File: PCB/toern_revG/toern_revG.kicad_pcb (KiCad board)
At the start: 4 copper layers, 160 x 71 mm, 97 parts, among them IC1 BQ24075TRGTR, J1 AudioJack3_Switch, J10 Conn_01x02, J11 Conn_01x05, J11.5 Conn_01x05, J12 Conn_01x05, J13 Conn_01x05, J14 Conn_01x05, J15 Conn_01x05, J16 BATTERY, J17 AudioJack3_Ground, J3 AudioJack3_Ground, J4 USB_C_Receptacle_USB2.0, J5 AudioJack3_Switch, J6 AudioJack3_Switch, J7 AudioJack3_Switch, J8 Micro_SD_Card, J9 Conn_01x03, U1 SPX3819M5-L-3-3, U10 01x05 Connector_PinSocket_2.5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, U11 01x05 Connector_PinSocket_2.5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, U12 01x05 Connector_PinSocket_2.5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, U13 PAM8403D, U2 SPX3819M5-L-1-8, U3 SGTL5000XNBA3, U4 TLP2361V4_E, U5 74LVC2G14, U6 Teensy4.1, U7 SPX3819M5-L-3-3, U9 01x05 Connector_PinSocket_2.5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

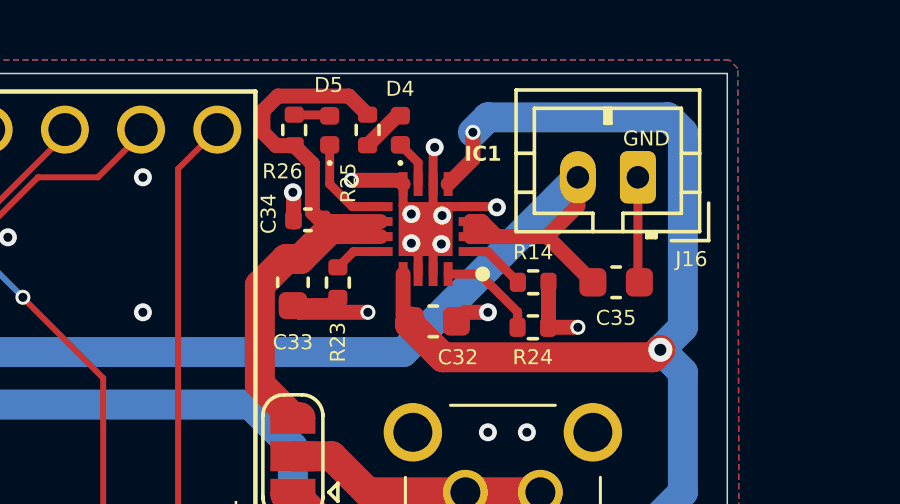
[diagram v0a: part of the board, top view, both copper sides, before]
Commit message: fixes for HD Displays 32x16
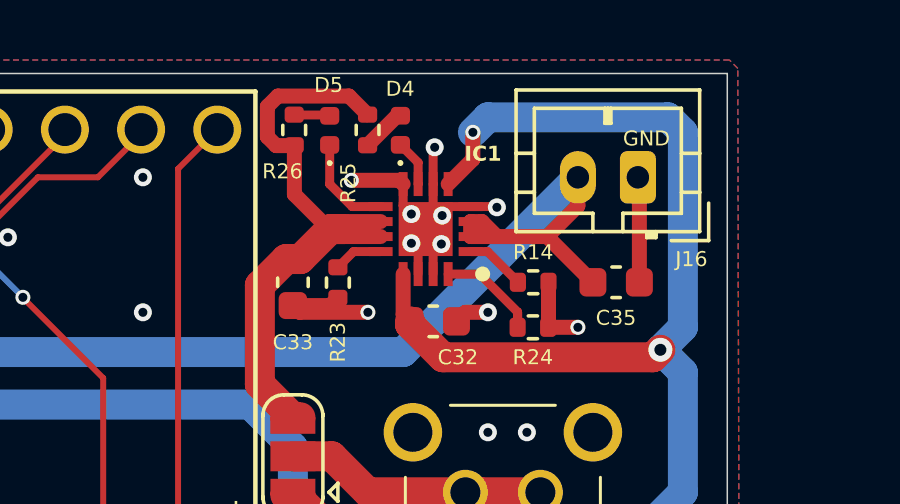
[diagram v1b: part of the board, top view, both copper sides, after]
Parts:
- removed C34: 100nF, Capacitor_SMD:C_0402_1005Metric
- C36: value 470µF -> 22µF
- D4: value Green -> Red
- D5: value Green -> Yellow
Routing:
- net GND: track 134.2 -> 133.3 mm, vias 157 -> 156
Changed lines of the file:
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@@
 			)
 		)
-		(property "lcsc#" "C19666 "
+		(property "lcsc#" "C1705"
 			(at 0 0 270)
 			(unlocked yes)
@@
 		)
 	)
-	(footprint "Capacitor_SMD:C_0402_1005Metric"
-		(layer "F.Cu")
-		(at 177 29.917727 180)
-		(descr "Capacitor SMD 0402 (1005 Metric), square (rectangular) end terminal, IPC-7351 nominal, (Body size source: IPC-SM-782 page 76, https://www.pcb-3d.com/wordpress/wp-content/uploads/ipc-sm-782a_amendment_1_and_2.pdf), generated with kicad-footprint-generator")
-		(tags "capacitor")
-		(property "Reference" "C34"
-			(at 1.308509 0.200909 270)
-			(layer "F.SilkS")
-			(effects
-				(font
-					(size 0.5 0.5)
-					(thickness 0.125)
-				)
-			)
-		)
-		(property "Value" "100nF"
-			(at 0 1.16 0)
-			(layer "F.Fab")
-			(effects
-				(font
-					(size 1 1)
-					(thickness 0.15)
-				)
-			)
-		)
-		(property "Datasheet" ""
-			(at 0 0 0)
-			(layer "F.Fab")
-			(hide yes)
-			(effects
-				(font
-					(size 1.27 1.27)
-					(thickness 0.15)
-				)
-			)
-		)
-		(property "Description" "Unpolarized capacitor, small symbol"
-			(at 0 0 0)
-			(layer "F.Fab")
-			(hide yes)
-			(effects
-				(font
-					(size 1.27 1.27)
-					(thickness 0.15)
-				)
-			)
-		)
-		(property "lcsc#" "C1525"
-			(at 0 0 270)
-			(unlocked yes)
-			(layer "F.Fab")
-			(hide yes)
-			(effects
-				(font
-					(size 1 1)
-					(thickness 0.15)
-				)
-			)
-		)
-		(property ki_fp_filters "C_*")
-		(sheetname "/")
-		(sheetfile "toern_revG.kicad_sch")
-		(attr smd)
-		(fp_line
-			(start -0.107836 0.36)
-			(end 0.107836 0.36)
-			(stroke
-				(width 0.12)
-				(type solid)
-			)
-			(layer "F.SilkS")
-		)
-		(fp_line
-			(start -0.107836 -0.36)
-			(end 0.107836 -0.36)
-			(stroke
-				(width 0.12)
-				(type solid)
-			)
-			(layer "F.SilkS")
-		)
-		(fp_line
-			(start 0.91 0.46)
-			(end -0.91 0.46)
-			(stroke
-				(width 0.05)
-				(type solid)
-			)
-			(layer "F.CrtYd")
-		)
-		(fp_line
-			(start 0.91 -0.46)
-			(end 0.91 0.46)
-			(stroke
-				(width 0.05)
-				(type solid)
-			)
-			(layer "F.CrtYd")
-		)
-		(fp_line
-			(start -0.91 0.46)
-			(end -0.91 -0.46)
-			(stroke
-				(width 0.05)
-				(type solid)
-			)
-			(layer "F.CrtYd")
-		)
-		(fp_line
-			(start -0.91 -0.46)
-			(end 0.91 -0.46)
-			(stroke
-				(width 0.05)
-				(type solid)
-			)
-			(layer "F.CrtYd")
-		)
-		(fp_line
-			(start 0.5 0.25)
-			(end -0.5 0.25)
-			(stroke
-				(width 0.1)
-				(type solid)
-			)
-			(layer "F.Fab")
-		)
-		(fp_line
-			(start 0.5 -0.25)
-			(end 0.5 0.25)
-			(stroke
-				(width 0.1)
-				(type solid)
-			)
-			(layer "F.Fab")
-		)
-		(fp_line
-			(start -0.5 0.25)
-			(end -0.5 -0.25)
-			(stroke
-				(width 0.1)
-				(type solid)
-			)
-			(layer "F.Fab")
-		)
-		(fp_line
-			(start -0.5 -0.25)
-			(end 0.5 -0.25)
-			(stroke
-				(width 0.1)
-				(type solid)
-			)
-			(layer "F.Fab")
-		)
-		(fp_text user "${REFERENCE}"
-			(at 0 0 0)
-			(layer "F.Fab")
-			(effects
-				(font
-					(size 0.25 0.25)
-					(thickness 0.04)
-				)
-			)
-		)
-		(pad "1" smd roundrect
-			(at -0.48 0 180)
-			(size 0.56 0.62)
-			(layers "F.Cu" "F.Mask" "F.Paste")
-			(roundrect_rratio 0.25)
-			(net 129 "VYS")
-			(pintype "passive")
-		)
-		(pad "2" smd roundrect
-			(at 0.48 0 180)
-			(size 0.56 0.62)
-			(layers "F.Cu" "F.Mask" "F.Paste")
-			(roundrect_rratio 0.25)
-			(net 1 "GND")
-			(pintype "passive")
-		)
-		(embedded_fonts no)
-		(model "${KICAD9_3DMODEL_DIR}/Capacitor_SMD.3dshapes/C_0402_1005Metric.wrl"
-			(offset
-				(xyz 0 0 0)
-			)
-			(scale
-				(xyz 1 1 1)
-			)
-			(rotate
-				(xyz 0 0 0)
-			)
-		)
-	)
 	(footprint "Capacitor_SMD:C_0603_1608Metric"
 		(layer "F.Cu")
@@
 			)
 		)
-		(property "Value" "Green"
+		(property "Value" "Yellow"
 			(at 0 1.17 90)
 			(layer "F.Fab")
@@
 			)
 		)
-		(property "lcsc#" "C2290"
+		(property "lcsc#" "C74342"
 			(at 0 0 0)
 			(unlocked yes)
@@
 			)
 		)
-		(property "Value" "470µF"
+		(property "Value" "22µF"
 			(at 0 1.43 0)
 			(layer "F.Fab")
@@
 			)
 		)
+		(property "lcsc#" "C1859"
+			(at 0 0 0)
+			(unlocked yes)
+			(layer "F.Fab")
+			(hide yes)
+			(effects
+				(font
+					(size 1 1)
+					(thickness 0.15)
+				)
+			)
+		)
 		(property ki_fp_filters "C_*")
 		(sheetname "/")
@@
 			)
 		)
-		(property "Value" "Green"
+		(property "Value" "Red"
 			(at 0 1.17 90)
 			(layer "F.Fab")
@@
 			)
 		)
-		(property "lcsc#" "C2286"
+		(property "lcsc#" "C71911"
 			(at 0 0 0)
 			(unlocked yes)
@@
 			)
 		)
-		(property "lcsc#" "C4961"
+		(property "lcsc#" "C25860"
 			(at 0 0 0)
 			(unlocked yes)
@@
 		(tags "capacitor")
 		(property "Reference" "C33"
-			(at 2 0 180)
+			(at 2 0 0)
 			(layer "F.SilkS")
 			(effects
@@
 			)
 		)
+		(property "lcsc#" "C25744"
+			(at 0 0 0)
+			(unlocked yes)
+			(layer "F.Fab")
+			(hide yes)
+			(effects
+				(font
+					(size 1 1)
+					(thickness 0.15)
+				)
+			)
+		)
 		(property ki_fp_filters "R_*")
 		(sheetname "/")
@@
 	)
 	(segment
-		(start 188 31.95)
-		(end 188 28.5)
-		(width 0.3)
-		(layer "F.Cu")
-		(net 1)
-	)
-	(segment
 		(start 181.175 27.551)
 		(end 181.175 28.725)
@@
 	)
 	(segment
-		(start 176.52 30)
-		(end 176.52 29.02)
-		(width 0.5)
-		(layer "F.Cu")
-		(net 1)
-	)
-	(segment
 		(start 183.275 29.475)
 		(end 183.3 29.5)
@@
 	)
 	(segment
+		(start 188.05 32)
+		(end 188.05 28.55)
+		(width 0.5)
+		(layer "F.Cu")
+		(net 1)
+	)
+	(segment
 		(start 136.65 48.69)
 		(end 137.6325 48.69)
@@
 	)
 	(segment
-		(start 176.52 29.02)
-		(end 176.5 29)
-		(width 0.5)
-		(layer "F.Cu")
-		(net 1)
-	)
-	(segment
 		(start 126.775 77.95)
 		(end 126.775 79.2)
@@
 	)
 	(segment
+		(start 188.05 28.55)
+		(end 188 28.5)
+		(width 0.5)
+		(layer "F.Cu")
+		(net 1)
+	)
+	(segment
 		(start 104 48.5)
 		(end 103.46 48.5)
@@
 	)
 	(via
-		(at 176.5 29)
-		(size 0.6)
-		(drill 0.3)
-		(layers "F.Cu" "B.Cu")
-		(free yes)
-		(net 1)
-	)
-	(via
 		(at 179 33)
 		(size 0.5)
@@
 	)
 	(segment
-		(start 175.5 27)
-		(end 175.5 26.291)
-		(width 0.5)
-		(layer "F.Cu")
-		(net 129)
-	)
-	(segment
-		(start 178.369022 25.791)
-		(end 178.99 26.411978)
+		(start 175.65 26.141)
+		(end 176 25.791)
 		(width 0.5)
 		(layer "F.Cu")
@@
 	(segment
 		(start 175.943109 27.443109)
-		(end 175.5 27)
+		(end 175.65 27.15)
 		(width 0.5)
 		(layer "F.Cu")
@@
 	)
 	(segment
-		(start 176.5442 27.443109)
-		(end 175.943109 27.443109)
-		(width 0.5)
-		(layer "F.Cu")
-		(net 129)
-	)
-	(segment
-		(start 175.5 26.291)
-		(end 176 25.791)
-		(width 0.5)
-		(layer "F.Cu")
-		(net 129)
-	)
-	(segment
-		(start 177.151 28.049909)
-		(end 176.5442 27.443109)
+		(start 176.55 29.07)
+		(end 176.55 27.448909)
 		(width 0.5)
 		(layer "F.Cu")
@@
 	)
 	(segment
-		(start 176 25.791)
-		(end 178.369022 25.791)
-		(width 0.5)
-		(layer "F.Cu")
-		(net 129)
-	)
-	(segment
 		(start 176.275 31.225)
 		(end 175.399 32.101)
@@
 	)
 	(segment
-		(start 177.151 29.671)
-		(end 177.151 28.049909)
+		(start 178.369022 25.791)
+		(end 178.99 26.411978)
+		(width 0.5)
+		(layer "F.Cu")
+		(net 129)
+	)
+	(segment
+		(start 175.65 27.15)
+		(end 175.65 26.141)
+		(width 0.5)
+		(layer "F.Cu")
+		(net 129)
+	)
+	(segment
+		(start 176.55 27.448909)
+		(end 176.5442 27.443109)
 		(width 0.5)
 		(layer "F.Cu")
@@
 	)
 	(segment
+		(start 176.5442 27.443109)
+		(end 175.943109 27.443109)
+		(width 0.5)
+		(layer "F.Cu")
+		(net 129)
+	)
+	(segment
 		(start 177.48 30)
-		(end 177.151 29.671)
+		(end 176.55 29.07)
+		(width 0.5)
+		(layer "F.Cu")
+		(net 129)
+	)
+	(segment
+		(start 176 25.791)
+		(end 178.369022 25.791)
 		(width 0.5)
 		(layer "F.Cu")

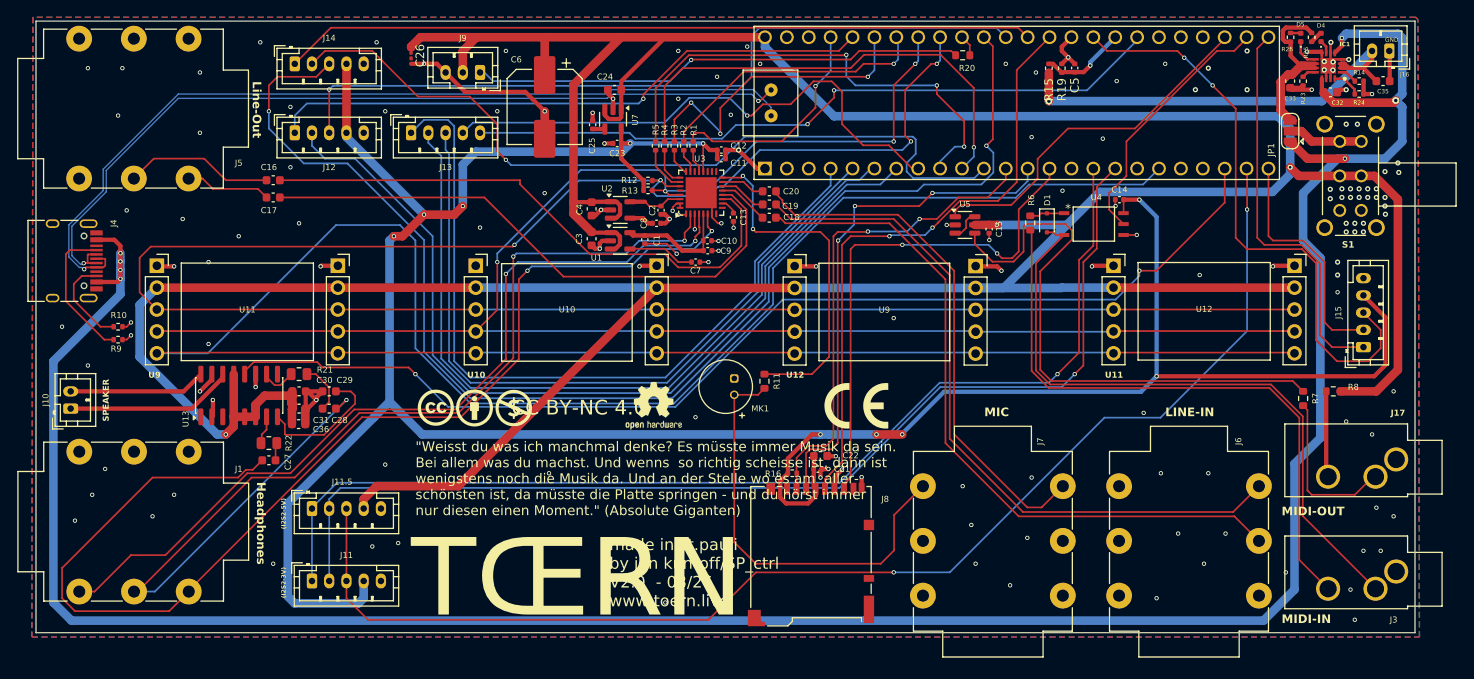
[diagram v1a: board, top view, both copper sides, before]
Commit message: extended reverb and muteAll fix for Draw==R
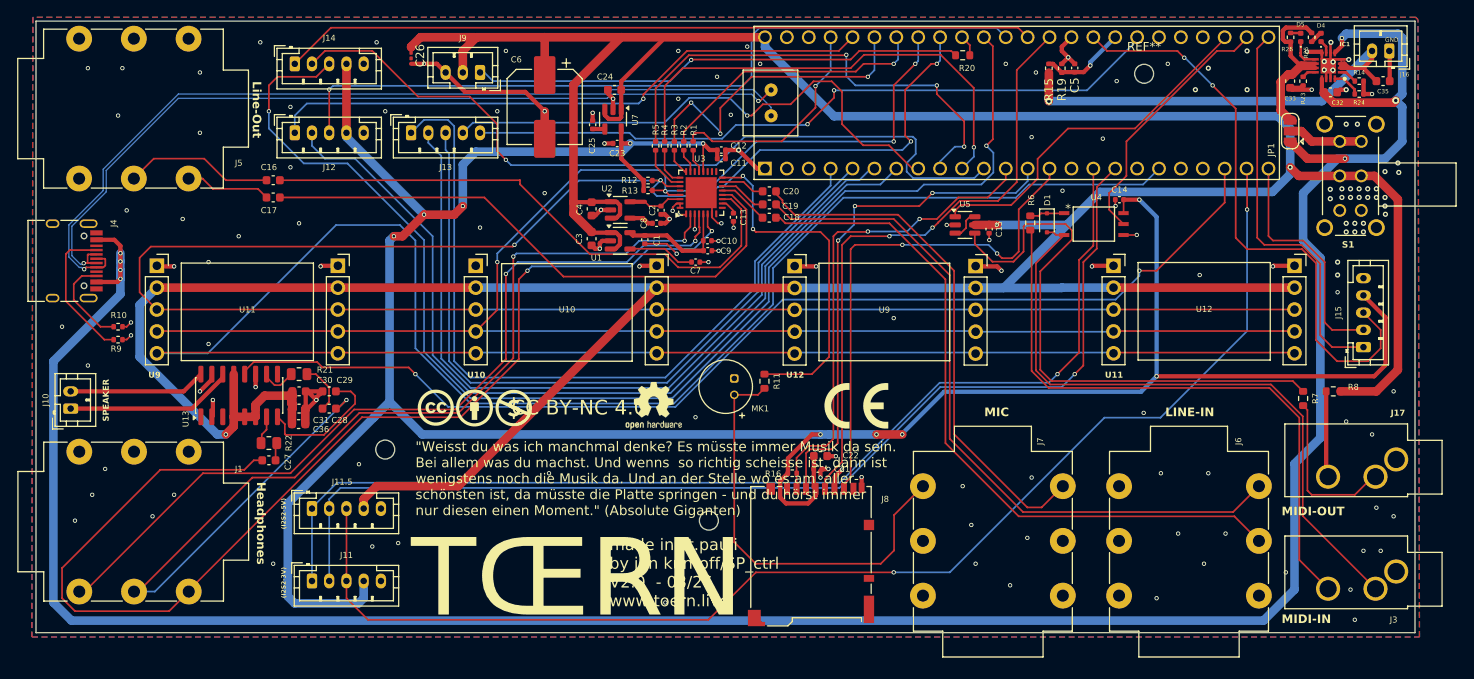
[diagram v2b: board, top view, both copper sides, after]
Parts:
- added Mounting: MountingHole_2.2mm_M2, MountingHole:MountingHole_2.2mm_M2, F.Cu at (109.0, 83.0)
- added REF**: MountingHole_2.2mm_M2, MountingHole:MountingHole_2.2mm_M2, F.Cu at (71.5, 74.8)
- added REF**: MountingHole_2.2mm_M2, MountingHole:MountingHole_2.2mm_M2, F.Cu at (159.6, 31.1)
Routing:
- net Net-(U3-HP_VGND): track 97.0 -> 98.0 mm
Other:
- board text removed: "${REFERENCE}"

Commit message: fixed PCB and shematics for RevG
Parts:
- removed Mounting, REF** (x2): MountingHole_2.2mm_M2, MountingHole:MountingHole_2.2mm_M2
- added MountingHole1: MountingHole_2.2mm_M2, MountingHole:MountingHole_2.2mm_M2, F.Cu at (71.5, 74.7)
- added MountingHole2: MountingHole_2.2mm_M2, MountingHole:MountingHole_2.2mm_M2, F.Cu at (109.0, 83.0)
- added MountingHole3: MountingHole_2.2mm_M2, MountingHole:MountingHole_2.2mm_M2, F.Cu at (159.6, 31.1)
- C26: footprint Capacitor_SMD:C_0201_0603Metric -> Capacitor_SMD:C_0603_1608Metric
- C29: value 0.1uF -> 100nF
- C5: footprint Capacitor_SMD:C_0402_1005Metric -> Capacitor_SMD:C_0603_1608Metric
- J16: value BATTERY -> Conn_01x02
- R11: value 2k2 -> 2.2k
- R23: value 1.11k -> 1.1k
- moved C26 7.14 mm to (81.3, 26.8), turned to 180 degrees
- moved J9 4.22 mm to (78.4, 30.0), turned to 0 degrees
- moved C5 0.42 mm to (151.6, 30.1)
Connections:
- J9 pad 2: +5V -> GND
- J9 pad 3: GND -> +5V
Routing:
- net +5V: track 498.3 -> 489.4 mm
- net Net-(J9-Pin_1): track 57.4 -> 61.9 mm
- net GND: track 133.3 -> 131.5 mm, vias 156 -> 154
- net VYS: track 22.4 -> 20.9 mm

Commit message: fixed PCB and shematics for RevG 2
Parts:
- removed U10, U11, U12, U9: 01x05 Connector_PinSocket_2.54mm, Connector_PinSocket_2.54mm:DuppaI2CEncoderV2.1
- added J18: Conn_01x05_Socket, Connector_PinSocket_2.54mm:PinSocket_1x05_P2.54mm_Vertical, F.Cu at (66.0, 53.4)
- added J19: Conn_01x05_Socket, Connector_PinSocket_2.54mm:PinSocket_1x05_P2.54mm_Vertical, F.Cu at (82.0, 53.4)
- added J2: Conn_01x05_Socket, Connector_PinSocket_2.54mm:PinSocket_1x05_P2.54mm_Vertical, F.Cu at (45.0, 53.4)
- added J20: Conn_01x05_Socket, Connector_PinSocket_2.54mm:PinSocket_1x05_P2.54mm_Vertical, F.Cu at (103.0, 53.4)
- added J21: Conn_01x05_Socket, Connector_PinSocket_2.54mm:PinSocket_1x05_P2.54mm_Vertical, F.Cu at (119.0, 53.4)
- added J22: Conn_01x05_Socket, Connector_PinSocket_2.54mm:PinSocket_1x05_P2.54mm_Vertical, F.Cu at (140.0, 53.4)
- added J23: Conn_01x05_Socket, Connector_PinSocket_2.54mm:PinSocket_1x05_P2.54mm_Vertical, F.Cu at (156.0, 53.4)
- added J24: Conn_01x05_Socket, Connector_PinSocket_2.54mm:PinSocket_1x05_P2.54mm_Vertical, F.Cu at (177.0, 53.4)
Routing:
- net 27_A13_SCK1: track 284.6 -> 285.4 mm
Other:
- board text removed: "U10"
- board text removed: "U12"
- board text removed: "U9"

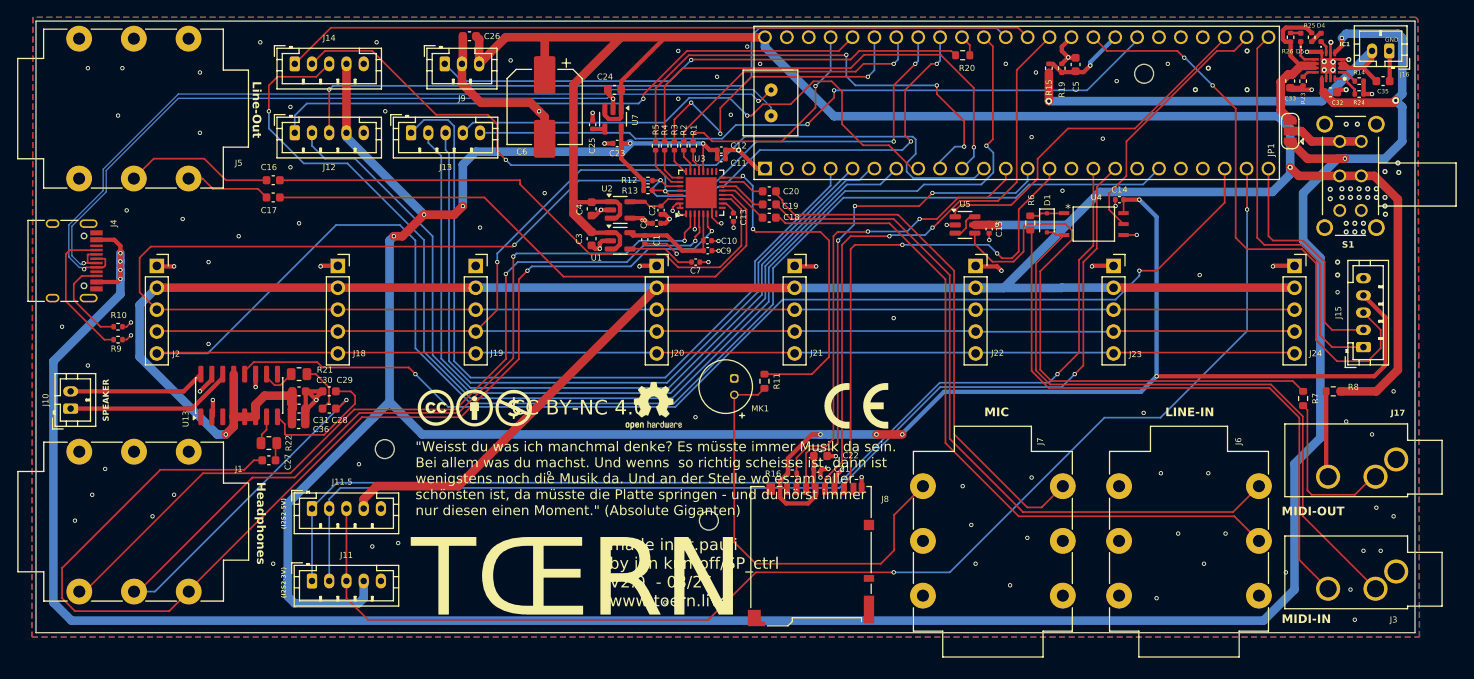
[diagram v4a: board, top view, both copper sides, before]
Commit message: better loading and saving speed and progress
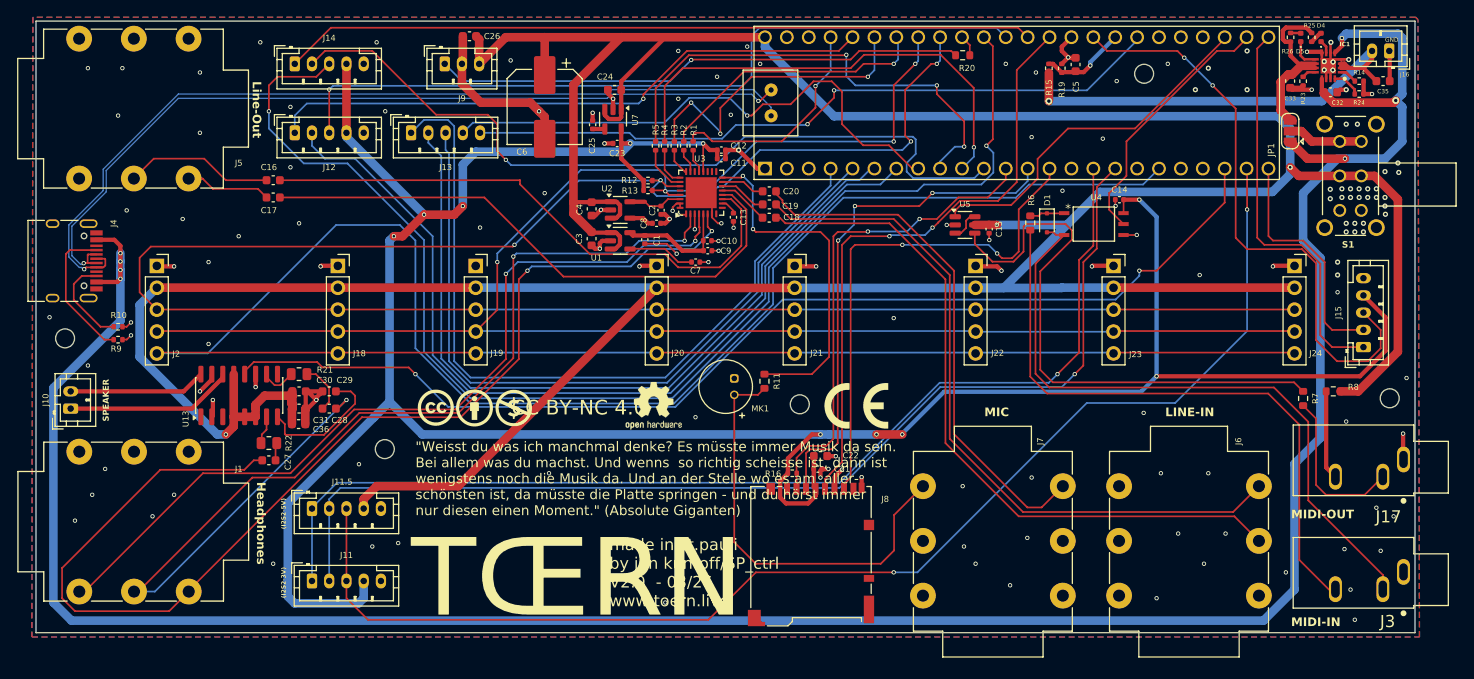
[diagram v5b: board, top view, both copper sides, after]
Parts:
- added MountingHole4: MountingHole_2.2mm_M2, MountingHole:MountingHole_2.2mm_M2, F.Cu at (34.4, 61.9)
- added MountingHole5: MountingHole_2.2mm_M2, MountingHole:MountingHole_2.2mm_M2, F.Cu at (188.1, 68.8)
- J17, J3: footprint Connector_Audio:Jack_3.5mm_CUI_SJ1-3533NG_Horizontal_CircularHoles -> SJ1-3533:CUI_SJ1-3533
- moved MountingHole2 17.1 mm to (119.6, 69.5)
- moved J3 0.85 mm to (189.7, 89.0), turned to 180 degrees
- moved J17 0.85 mm to (189.7, 75.9), turned to 180 degrees
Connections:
- R6 pad 2: Net-(J3-PadR) -> Net-(J3-Pad3)
- R7 pad 2: Net-(J17-PadT) -> Net-(J17-Pad2)
- R8 pad 1: Net-(J17-PadR) -> Net-(J17-Pad3)
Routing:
- net Net-(J3-Pad3): track 0.00 -> 71.1 mm
- net Net-(J3-PadR): track 71.1 -> 0.00 mm
- net Net-(J17-PadT): track 19.0 -> 0.00 mm
- net Net-(J17-Pad2): track 0.00 -> 18.9 mm
- net Net-(J17-Pad3): track 0.00 -> 10.3 mm
- net Net-(J17-PadR): track 9.99 -> 0.00 mm
- net GND: track 131.5 -> 134.5 mm
- net +5V: track 489.4 -> 488.2 mm
- net +3.3V: track 312.0 -> 311.0 mm
- net Net-(D1-A): track 75.9 -> 76.6 mm
